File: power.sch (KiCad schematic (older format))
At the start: 10 parts, among them U301 lm2575, U302 LM78L33

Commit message: Changed a bit, and did a full re-route
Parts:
- added TP301, TP302: TEST, Measurement_Points:Measurement_Point_Round-SMD-Pad_Big, symbol TEST
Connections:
- net +3V3: now also TP302.1
- net +5V: now also TP301.1
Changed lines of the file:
@@
 $EndComp
 $Comp
-L +3V3 #PWR027
+L +3V3 #PWR026
 U 1 1 585450B5
 P 5925 2025
-F 0 "#PWR027" H 5925 1875 50  0001 C CNN
+F 0 "#PWR026" H 5925 1875 50  0001 C CNN
 F 1 "+3V3" H 5925 2165 50  0000 C CNN
 F 2 "" H 5925 2025 50  0000 C CNN
@@
 $EndComp
 $Comp
-L GND #PWR028
+L GND #PWR027
 U 1 1 585450C3
 P 5275 2600
-F 0 "#PWR028" H 5275 2350 50  0001 C CNN
+F 0 "#PWR027" H 5275 2350 50  0001 C CNN
 F 1 "GND" H 5275 2450 50  0000 C CNN
 F 2 "" H 5275 2600 50  0000 C CNN
@@
 $EndComp
 $Comp
-L +5V #PWR029
+L +5V #PWR028
 U 1 1 585450FC
 P 4325 2025
-F 0 "#PWR029" H 4325 1875 50  0001 C CNN
+F 0 "#PWR028" H 4325 1875 50  0001 C CNN
 F 1 "+5V" H 4325 2165 50  0000 C CNN
 F 2 "" H 4325 2025 50  0000 C CNN
@@
 $EndComp
 $Comp
-L VDDA #PWR030
+L VDDA #PWR029
 U 1 1 58545105
 P 7650 2025
-F 0 "#PWR030" H 7650 1875 50  0001 C CNN
+F 0 "#PWR029" H 7650 1875 50  0001 C CNN
 F 1 "VDDA" H 7650 2175 50  0000 C CNN
 F 2 "" H 7650 2025 50  0000 C CNN
@@
 $EndComp
 $Comp
-L GNDA #PWR031
+L GNDA #PWR030
 U 1 1 5854511E
 P 7650 2750
-F 0 "#PWR031" H 7650 2500 50  0001 C CNN
+F 0 "#PWR030" H 7650 2500 50  0001 C CNN
 F 1 "GNDA" H 7650 2600 50  0000 C CNN
 F 2 "" H 7650 2750 50  0000 C CNN
@@
 mic5205
 $Comp
-L GND #PWR032
+L GND #PWR031
 U 1 1 5857240C
 P 3375 3025
-F 0 "#PWR032" H 3375 2775 50  0001 C CNN
+F 0 "#PWR031" H 3375 2775 50  0001 C CNN
 F 1 "GND" H 3375 2875 50  0000 C CNN
 F 2 "" H 3375 3025 50  0000 C CNN
@@
 $EndComp
 $Comp
-L +24V #PWR033
+L +24V #PWR032
 U 1 1 585729CA
 P 1925 2300
-F 0 "#PWR033" H 1925 2150 50  0001 C CNN
+F 0 "#PWR032" H 1925 2150 50  0001 C CNN
 F 1 "+24V" H 1925 2440 50  0000 C CNN
 F 2 "" H 1925 2300 50  0000 C CNN
@@
 $EndComp
 $Comp
-L GND #PWR034
+L GND #PWR033
 U 1 1 585729F2
 P 1925 2600
-F 0 "#PWR034" H 1925 2350 50  0001 C CNN
+F 0 "#PWR033" H 1925 2350 50  0001 C CNN
 F 1 "GND" H 1925 2450 50  0000 C CNN
 F 2 "" H 1925 2600 50  0000 C CNN
@@
 	1    0    0    -1
 $EndComp
+$Comp
+L TEST TP301
+U 1 1 58600192
+P 3875 2300
+F 0 "TP301" H 3875 2600 50  0000 C BNN
+F 1 "TEST" H 3875 2550 50  0000 C CNN
+F 2 "Measurement_Points:Measurement_Point_Round-SMD-Pad_Big" H 3875 2300 50  0001 C CNN
+F 3 "" H 3875 2300 50  0000 C CNN
+	1    3875 2300
+	1    0    0    -1
+$EndComp
+$Comp
+L TEST TP302
+U 1 1 5860025B
+P 6100 2300
+F 0 "TP302" H 6100 2600 50  0000 C BNN
+F 1 "TEST" H 6100 2550 50  0000 C CNN
+F 2 "Measurement_Points:Measurement_Point_Round-SMD-Pad_Big" H 6100 2300 50  0001 C CNN
+F 3 "" H 6100 2300 50  0000 C CNN
+	1    6100 2300
+	1    0    0    -1
+$EndComp
+Connection ~ 6100 2300
 $EndSCHEMATC

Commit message: Routed for 5x5 pcb
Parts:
- removed U302: LM78L33, TO_SOT_Packages_SMD:SOT89-3_Housing_Handsoldering, symbol LM78L33
- added U302: mic5205, TO_SOT_Packages_SMD:SOT-23-5, symbol mic5205
- C305: value 1u -> 2u
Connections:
- net +3V3: now also U302.5 (OUT)
- net +5V: now also U302.1 (IN), U302.3 (en)
- net GND: now also U302.2 (GND)
- no-connect marks 0 -> 1
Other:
- moved on the sheet: C305
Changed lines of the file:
@@
 EESchema Schematic File Version 2
+LIBS:linearPower
 LIBS:power
 LIBS:device
@@
 $EndDescr
 $Comp
-L LM78L33 U302
-U 1 1 585450AE
-P 5275 2350
-F 0 "U302" H 5075 2550 50  0000 C CNN
-F 1 "LM78L33" H 5275 2550 50  0000 L CNN
-F 2 "TO_SOT_Packages_SMD:SOT89-3_Housing_Handsoldering" H 5275 2450 50  0001 C CIN
-F 3 "" H 5275 2350 50  0000 C CNN
-	1    5275 2350
-	1    0    0    -1
-$EndComp
-$Comp
-L +3V3 #PWR026
+L +3V3 #PWR306
 U 1 1 585450B5
 P 5925 2025
-F 0 "#PWR026" H 5925 1875 50  0001 C CNN
+F 0 "#PWR306" H 5925 1875 50  0001 C CNN
 F 1 "+3V3" H 5925 2165 50  0000 C CNN
 F 2 "" H 5925 2025 50  0000 C CNN
@@
 $EndComp
 $Comp
-L GND #PWR027
+L GND #PWR305
 U 1 1 585450C3
 P 5275 2600
-F 0 "#PWR027" H 5275 2350 50  0001 C CNN
+F 0 "#PWR305" H 5275 2350 50  0001 C CNN
 F 1 "GND" H 5275 2450 50  0000 C CNN
 F 2 "" H 5275 2600 50  0000 C CNN
@@
 L C C305
 U 1 1 585450D2
-P 5800 2450
-F 0 "C305" H 5825 2550 50  0000 L CNN
-F 1 "1u" H 5825 2350 50  0000 L CNN
-F 2 "Capacitors_SMD:C_0805_HandSoldering" H 5838 2300 50  0001 C CNN
-F 3 "" H 5800 2450 50  0000 C CNN
-	1    5800 2450
-	1    0    0    -1
-$EndComp
-$Comp
-L +5V #PWR028
+P 5925 2450
+F 0 "C305" H 5950 2550 50  0000 L CNN
+F 1 "2u" H 5950 2350 50  0000 L CNN
+F 2 "Capacitors_SMD:C_0805_HandSoldering" H 5963 2300 50  0001 C CNN
+F 3 "" H 5925 2450 50  0000 C CNN
+	1    5925 2450
+	1    0    0    -1
+$EndComp
+$Comp
+L +5V #PWR304
 U 1 1 585450FC
 P 4325 2025
-F 0 "#PWR028" H 4325 1875 50  0001 C CNN
+F 0 "#PWR304" H 4325 1875 50  0001 C CNN
 F 1 "+5V" H 4325 2165 50  0000 C CNN
 F 2 "" H 4325 2025 50  0000 C CNN
@@
 $EndComp
 $Comp
-L VDDA #PWR029
+L VDDA #PWR307
 U 1 1 58545105
 P 7650 2025
-F 0 "#PWR029" H 7650 1875 50  0001 C CNN
+F 0 "#PWR307" H 7650 1875 50  0001 C CNN
 F 1 "VDDA" H 7650 2175 50  0000 C CNN
 F 2 "" H 7650 2025 50  0000 C CNN
@@
 $EndComp
 $Comp
-L GNDA #PWR030
+L GNDA #PWR308
 U 1 1 5854511E
 P 7650 2750
-F 0 "#PWR030" H 7650 2500 50  0001 C CNN
+F 0 "#PWR308" H 7650 2500 50  0001 C CNN
 F 1 "GNDA" H 7650 2600 50  0000 C CNN
 F 2 "" H 7650 2750 50  0000 C CNN
@@
 mic5205
 $Comp
-L GND #PWR031
+L GND #PWR303
 U 1 1 5857240C
 P 3375 3025
-F 0 "#PWR031" H 3375 2775 50  0001 C CNN
+F 0 "#PWR303" H 3375 2775 50  0001 C CNN
 F 1 "GND" H 3375 2875 50  0000 C CNN
 F 2 "" H 3375 3025 50  0000 C CNN
@@
 $EndComp
 $Comp
-L +24V #PWR032
+L +24V #PWR301
 U 1 1 585729CA
 P 1925 2300
-F 0 "#PWR032" H 1925 2150 50  0001 C CNN
+F 0 "#PWR301" H 1925 2150 50  0001 C CNN
 F 1 "+24V" H 1925 2440 50  0000 C CNN
 F 2 "" H 1925 2300 50  0000 C CNN
@@
 $EndComp
 $Comp
-L GND #PWR033
+L GND #PWR302
 U 1 1 585729F2
 P 1925 2600
-F 0 "#PWR033" H 1925 2350 50  0001 C CNN
+F 0 "#PWR302" H 1925 2350 50  0001 C CNN
 F 1 "GND" H 1925 2450 50  0000 C CNN
 F 2 "" H 1925 2600 50  0000 C CNN
@@
 Wire Wire Line
 	3875 2600 6300 2600
-Connection ~ 5800 2300
+Connection ~ 5925 2300
 Connection ~ 5275 2600
 Wire Wire Line
@@
 Wire Wire Line
 	5925 2300 5925 2025
-Connection ~ 5925 2300
 Wire Wire Line
 	7300 2300 7650 2300
@@
 Wire Wire Line
 	7300 2600 7650 2600
-Connection ~ 5800 2600
+Connection ~ 5925 2600
 Wire Wire Line
 	7650 2600 7650 2750
@@
 	1    0    0    -1
 $EndComp
+Connection ~ 6100 2300
 $Comp
 L TEST TP302
@@
 	1    0    0    -1
 $EndComp
-Connection ~ 6100 2300
+$Comp
+L mic5205 U302
+U 1 1 58803724
+P 5275 2350
+F 0 "U302" H 5075 2550 50  0000 C CNN
+F 1 "mic5205" H 5275 2550 50  0000 L CNN
+F 2 "TO_SOT_Packages_SMD:SOT-23-5" H 5275 2450 50  0001 C CIN
+F 3 "" H 5075 2550 50  0000 C CNN
+	1    5275 2350
+	1    0    0    -1
+$EndComp
+Wire Wire Line
+	4875 2300 4875 2450
+NoConn ~ 5675 2450
 $EndSCHEMATC

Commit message: Rerouted, and made everything beautifull
 - added screw bolt-holes for the output.
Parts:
- C301: footprint Capacitors_ThroughHole:C_Radial_D8_L21_P3.8 -> Capacitors_ThroughHole:CP_Radial_D10.0mm_P2.50mm
- C302: footprint Capacitors_ThroughHole:C_Radial_D8_L11.5_P3.5 -> Capacitors_ThroughHole:CP_Radial_D8.0mm_P5.00mm
- D301: footprint Diodes_ThroughHole:Diode_DO-41_SOD81_Vertical_KathodeUp -> Diodes_ThroughHole:D_DO-41_SOD81_P5.08mm_Vertical_KathodeUp
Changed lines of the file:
@@
 $EndDescr
 $Comp
-L +3V3 #PWR306
+L +3V3 #PWR033
 U 1 1 585450B5
 P 5925 2025
-F 0 "#PWR306" H 5925 1875 50  0001 C CNN
+F 0 "#PWR033" H 5925 1875 50  0001 C CNN
 F 1 "+3V3" H 5925 2165 50  0000 C CNN
 F 2 "" H 5925 2025 50  0000 C CNN
@@
 $EndComp
 $Comp
-L GND #PWR305
+L GND #PWR034
 U 1 1 585450C3
 P 5275 2600
-F 0 "#PWR305" H 5275 2350 50  0001 C CNN
+F 0 "#PWR034" H 5275 2350 50  0001 C CNN
 F 1 "GND" H 5275 2450 50  0000 C CNN
 F 2 "" H 5275 2600 50  0000 C CNN
@@
 $EndComp
 $Comp
-L +5V #PWR304
+L +5V #PWR035
 U 1 1 585450FC
 P 4325 2025
-F 0 "#PWR304" H 4325 1875 50  0001 C CNN
+F 0 "#PWR035" H 4325 1875 50  0001 C CNN
 F 1 "+5V" H 4325 2165 50  0000 C CNN
 F 2 "" H 4325 2025 50  0000 C CNN
@@
 $EndComp
 $Comp
-L VDDA #PWR307
+L VDDA #PWR036
 U 1 1 58545105
 P 7650 2025
-F 0 "#PWR307" H 7650 1875 50  0001 C CNN
+F 0 "#PWR036" H 7650 1875 50  0001 C CNN
 F 1 "VDDA" H 7650 2175 50  0000 C CNN
 F 2 "" H 7650 2025 50  0000 C CNN
@@
 $EndComp
 $Comp
-L GNDA #PWR308
+L GNDA #PWR037
 U 1 1 5854511E
 P 7650 2750
-F 0 "#PWR308" H 7650 2500 50  0001 C CNN
+F 0 "#PWR037" H 7650 2500 50  0001 C CNN
 F 1 "GNDA" H 7650 2600 50  0000 C CNN
 F 2 "" H 7650 2750 50  0000 C CNN
@@
 mic5205
 $Comp
-L GND #PWR303
+L GND #PWR038
 U 1 1 5857240C
 P 3375 3025
-F 0 "#PWR303" H 3375 2775 50  0001 C CNN
+F 0 "#PWR038" H 3375 2775 50  0001 C CNN
 F 1 "GND" H 3375 2875 50  0000 C CNN
 F 2 "" H 3375 3025 50  0000 C CNN
@@
 F 0 "D301" H 3375 2925 50  0000 C CNN
 F 1 "D_Schottky" H 3375 2725 50  0000 C CNN
-F 2 "Diodes_ThroughHole:Diode_DO-41_SOD81_Vertical_KathodeUp" H 3375 2825 50  0001 C CNN
+F 2 "Diodes_ThroughHole:D_DO-41_SOD81_P5.08mm_Vertical_KathodeUp" H 3375 2825 50  0001 C CNN
 F 3 "" H 3375 2825 50  0000 C CNN
 	1    3375 2825
@@
 F 0 "C302" H 3900 2550 50  0000 L CNN
 F 1 "100uF" H 3900 2350 50  0000 L CNN
-F 2 "Capacitors_ThroughHole:C_Radial_D8_L11.5_P3.5" H 3913 2300 50  0001 C CNN
+F 2 "Capacitors_ThroughHole:CP_Radial_D8.0mm_P5.00mm" H 3913 2300 50  0001 C CNN
 F 3 "" H 3875 2450 50  0000 C CNN
 	1    3875 2450
@@
 F 0 "C301" H 1950 2550 50  0000 L CNN
 F 1 "100uF" H 1950 2350 50  0000 L CNN
-F 2 "Capacitors_ThroughHole:C_Radial_D8_L21_P3.8" H 1963 2300 50  0001 C CNN
+F 2 "Capacitors_ThroughHole:CP_Radial_D10.0mm_P2.50mm" H 1963 2300 50  0001 C CNN
 F 3 "" H 1925 2450 50  0000 C CNN
 	1    1925 2450
@@
 $EndComp
 $Comp
-L +24V #PWR301
+L +24V #PWR039
 U 1 1 585729CA
 P 1925 2300
-F 0 "#PWR301" H 1925 2150 50  0001 C CNN
+F 0 "#PWR039" H 1925 2150 50  0001 C CNN
 F 1 "+24V" H 1925 2440 50  0000 C CNN
 F 2 "" H 1925 2300 50  0000 C CNN
@@
 $EndComp
 $Comp
-L GND #PWR302
+L GND #PWR040
 U 1 1 585729F2
 P 1925 2600
-F 0 "#PWR302" H 1925 2350 50  0001 C CNN
+F 0 "#PWR040" H 1925 2350 50  0001 C CNN
 F 1 "GND" H 1925 2450 50  0000 C CNN
 F 2 "" H 1925 2600 50  0000 C CNN

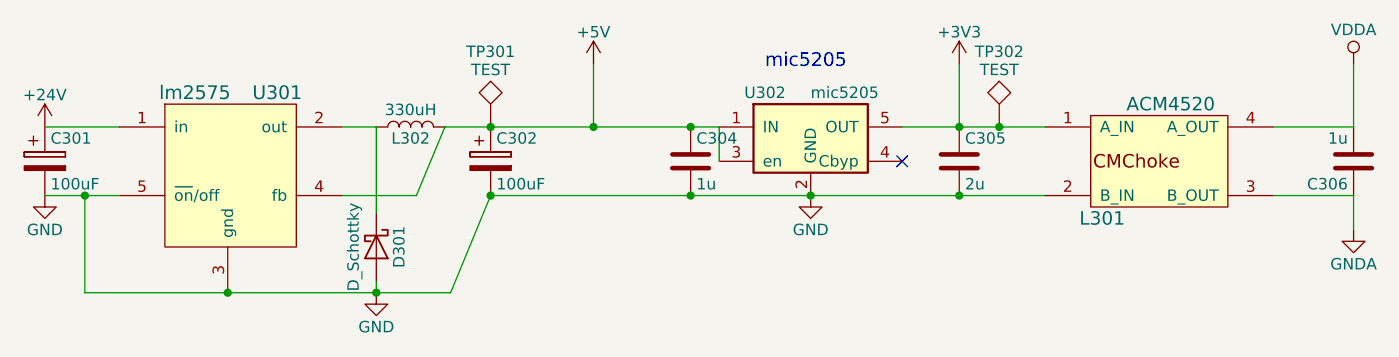
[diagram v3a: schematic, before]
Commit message: Added small display.
And made everything look even nicer
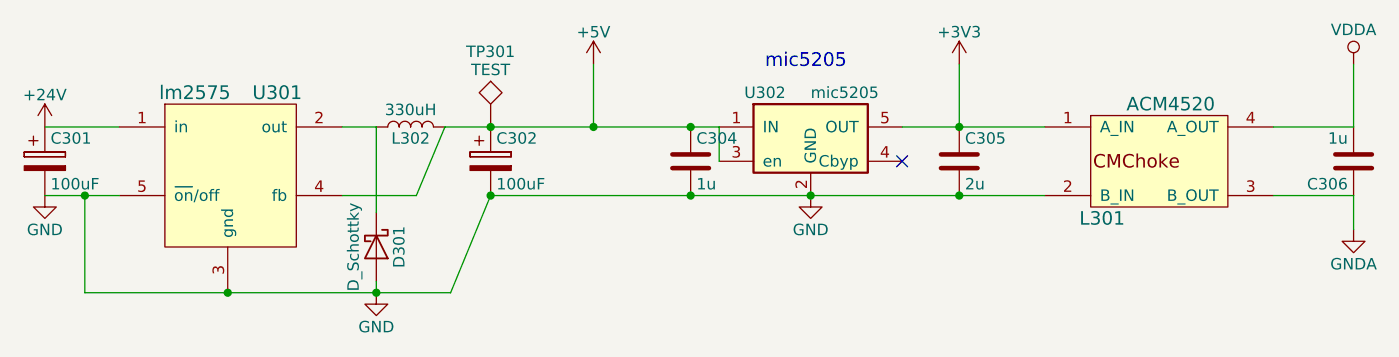
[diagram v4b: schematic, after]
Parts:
- removed TP302: TEST, Measurement_Points:Measurement_Point_Round-SMD-Pad_Big, symbol TEST
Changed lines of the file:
@@
 LIBS:valves
 LIBS:stm32
-LIBS:main-cache
-LIBS:io-cache
 LIBS:mppt-cache
 EELAYER 25 0
@@
 $Descr A4 11693 8268
 encoding utf-8
-Sheet 3 3
+Sheet 3 4
 Title ""
 Date ""
@@
 $EndDescr
 $Comp
-L +3V3 #PWR033
+L +3V3 #PWR030
 U 1 1 585450B5
 P 5925 2025
-F 0 "#PWR033" H 5925 1875 50  0001 C CNN
+F 0 "#PWR030" H 5925 1875 50  0001 C CNN
 F 1 "+3V3" H 5925 2165 50  0000 C CNN
 F 2 "" H 5925 2025 50  0000 C CNN
@@
 $EndComp
 $Comp
-L GND #PWR034
+L GND #PWR031
 U 1 1 585450C3
 P 5275 2600
-F 0 "#PWR034" H 5275 2350 50  0001 C CNN
+F 0 "#PWR031" H 5275 2350 50  0001 C CNN
 F 1 "GND" H 5275 2450 50  0000 C CNN
 F 2 "" H 5275 2600 50  0000 C CNN
@@
 $EndComp
 $Comp
-L +5V #PWR035
+L +5V #PWR032
 U 1 1 585450FC
 P 4325 2025
-F 0 "#PWR035" H 4325 1875 50  0001 C CNN
+F 0 "#PWR032" H 4325 1875 50  0001 C CNN
 F 1 "+5V" H 4325 2165 50  0000 C CNN
 F 2 "" H 4325 2025 50  0000 C CNN
@@
 $EndComp
 $Comp
-L VDDA #PWR036
+L VDDA #PWR033
 U 1 1 58545105
 P 7650 2025
-F 0 "#PWR036" H 7650 1875 50  0001 C CNN
+F 0 "#PWR033" H 7650 1875 50  0001 C CNN
 F 1 "VDDA" H 7650 2175 50  0000 C CNN
 F 2 "" H 7650 2025 50  0000 C CNN
@@
 $EndComp
 $Comp
-L GNDA #PWR037
+L GNDA #PWR034
 U 1 1 5854511E
 P 7650 2750
-F 0 "#PWR037" H 7650 2500 50  0001 C CNN
+F 0 "#PWR034" H 7650 2500 50  0001 C CNN
 F 1 "GNDA" H 7650 2600 50  0000 C CNN
 F 2 "" H 7650 2750 50  0000 C CNN
@@
 mic5205
 $Comp
-L GND #PWR038
+L GND #PWR035
 U 1 1 5857240C
 P 3375 3025
-F 0 "#PWR038" H 3375 2775 50  0001 C CNN
+F 0 "#PWR035" H 3375 2775 50  0001 C CNN
 F 1 "GND" H 3375 2875 50  0000 C CNN
 F 2 "" H 3375 3025 50  0000 C CNN
@@
 $EndComp
 $Comp
-L +24V #PWR039
+L +24V #PWR036
 U 1 1 585729CA
 P 1925 2300
-F 0 "#PWR039" H 1925 2150 50  0001 C CNN
+F 0 "#PWR036" H 1925 2150 50  0001 C CNN
 F 1 "+24V" H 1925 2440 50  0000 C CNN
 F 2 "" H 1925 2300 50  0000 C CNN
@@
 $EndComp
 $Comp
-L GND #PWR040
+L GND #PWR037
 U 1 1 585729F2
 P 1925 2600
-F 0 "#PWR040" H 1925 2350 50  0001 C CNN
+F 0 "#PWR037" H 1925 2350 50  0001 C CNN
 F 1 "GND" H 1925 2450 50  0000 C CNN
 F 2 "" H 1925 2600 50  0000 C CNN
@@
 	1    0    0    -1
 $EndComp
-Connection ~ 6100 2300
-$Comp
-L TEST TP302
-U 1 1 5860025B
-P 6100 2300
-F 0 "TP302" H 6100 2600 50  0000 C BNN
-F 1 "TEST" H 6100 2550 50  0000 C CNN
-F 2 "Measurement_Points:Measurement_Point_Round-SMD-Pad_Big" H 6100 2300 50  0001 C CNN
-F 3 "" H 6100 2300 50  0000 C CNN
-	1    6100 2300
-	1    0    0    -1
-$EndComp
